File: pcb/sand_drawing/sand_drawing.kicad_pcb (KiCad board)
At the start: 2 copper layers, 34 parts, among them J0 12V GND, J1 Stepper1, J2 Stepper2, J3 Opto 1, J4 Opto 2, J5 UART, SW1 EN, SW2 IO0, U2 AMS1117-3.3, U3 ESP32-WROOM-32D

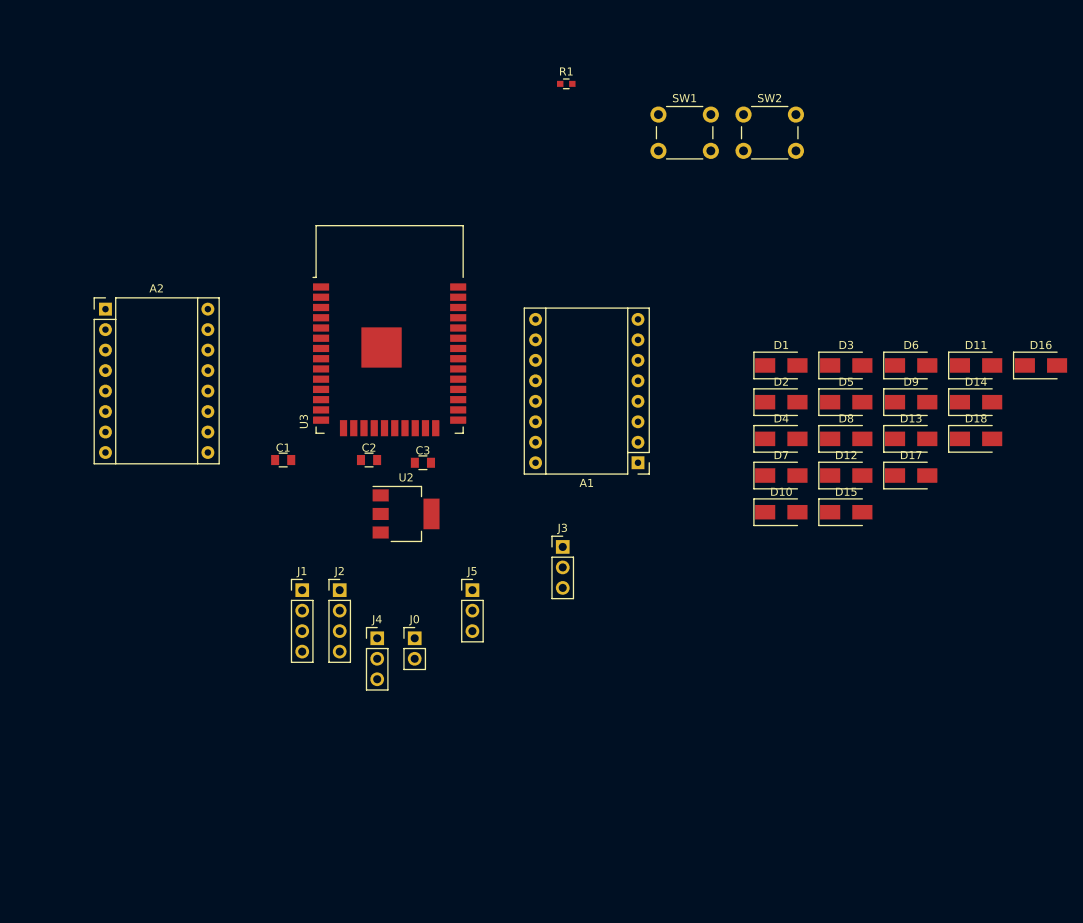
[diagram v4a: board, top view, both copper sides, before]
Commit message: Update BOM and beginning to lay out the new PCB.
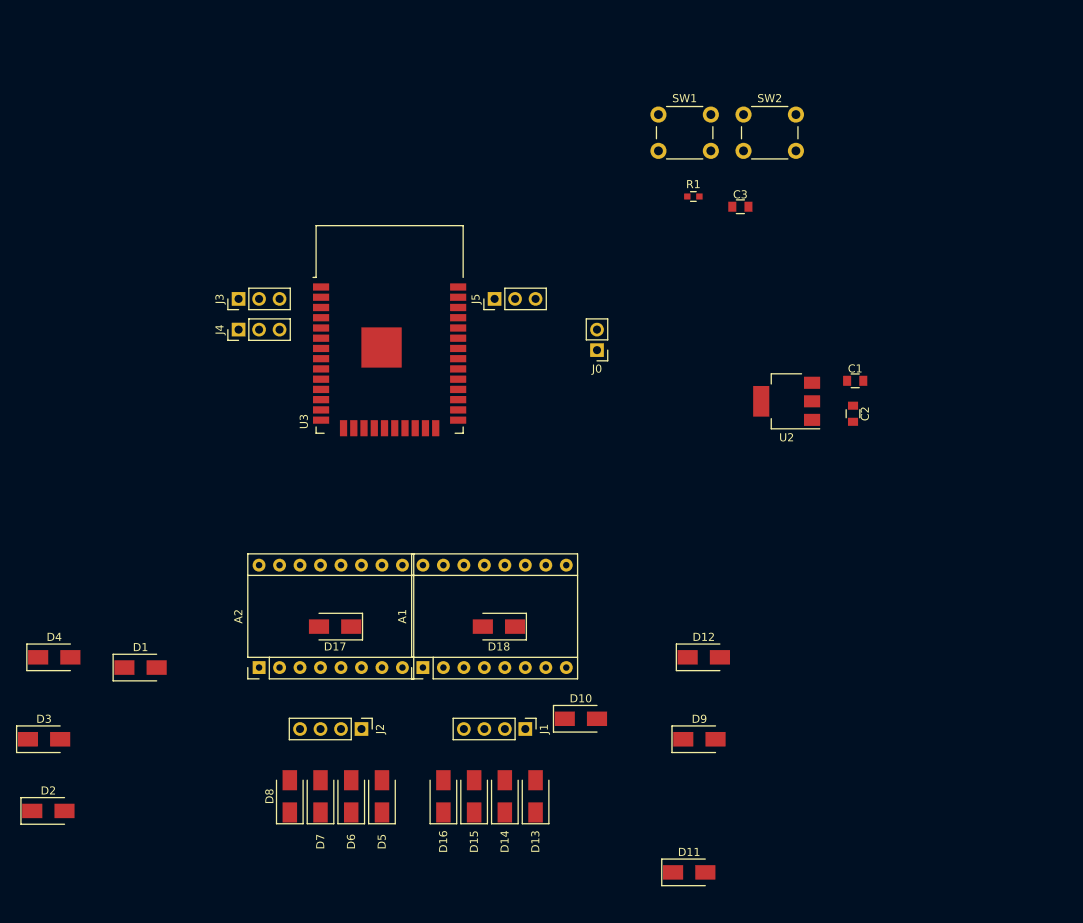
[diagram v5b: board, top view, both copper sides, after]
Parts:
- moved D3 109.8 mm to (81.3, 152.4)
- moved D2 104.1 mm to (81.8, 161.3)
- moved D4 94.2 mm to (82.5, 142.2)
- moved D16 91.4 mm to (130.8, 159.5), turned to 90 degrees
- moved D1 87.9 mm to (93.2, 143.5)
- moved D6 87.6 mm to (119.4, 159.5), turned to 90 degrees
- moved D8 82.0 mm to (111.8, 159.5), turned to 90 degrees
- moved D14 76.2 mm to (138.4, 159.5), turned to 90 degrees
- moved D5 75.5 mm to (123.2, 159.5), turned to 90 degrees
- moved D17 73.9 mm to (117.4, 138.4), turned to 180 degrees
- moved D11 72.2 mm to (161.3, 168.9)
- moved C1 71.6 mm to (181.9, 108.0)
- moved D7 69.6 mm to (115.6, 159.5), turned to 90 degrees
- moved D13 64.3 mm to (142.2, 159.5), turned to 90 degrees
- moved D18 63.6 mm to (137.7, 138.4), turned to 180 degrees
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
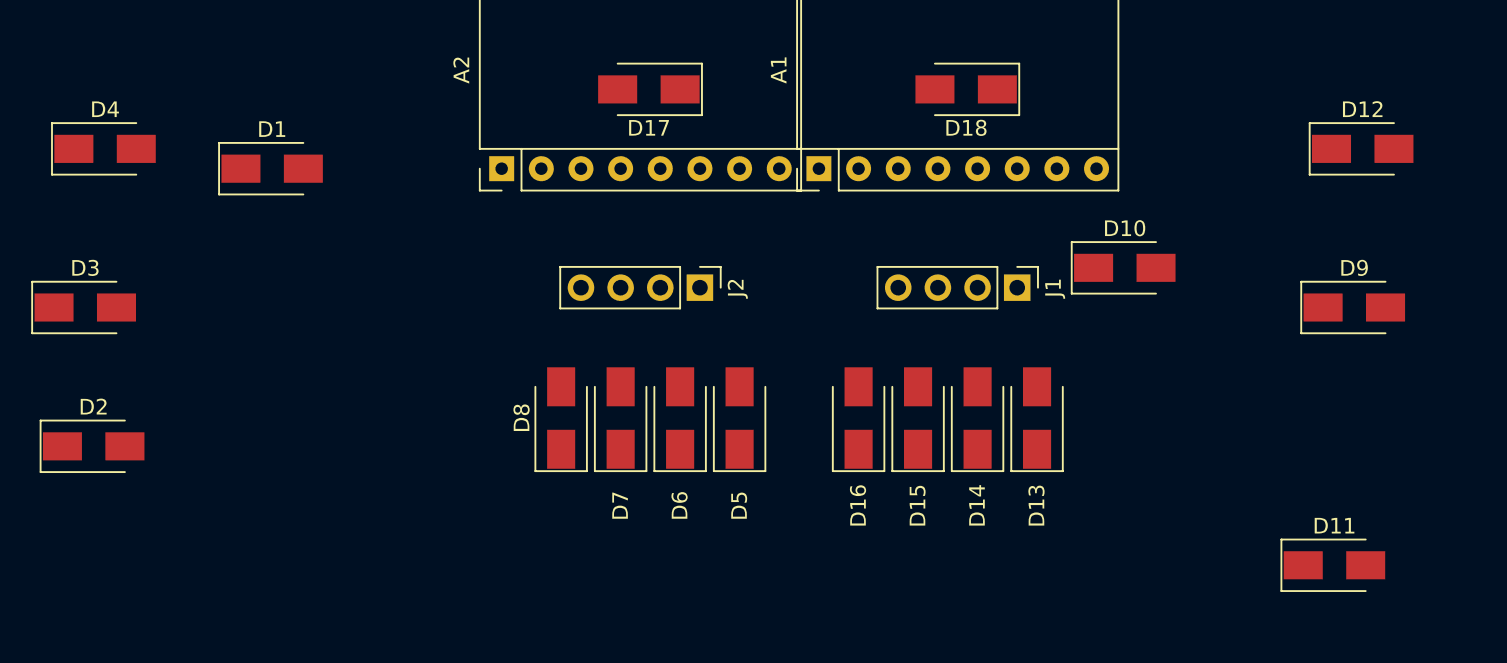
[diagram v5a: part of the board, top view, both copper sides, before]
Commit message: Protection diodes placed.
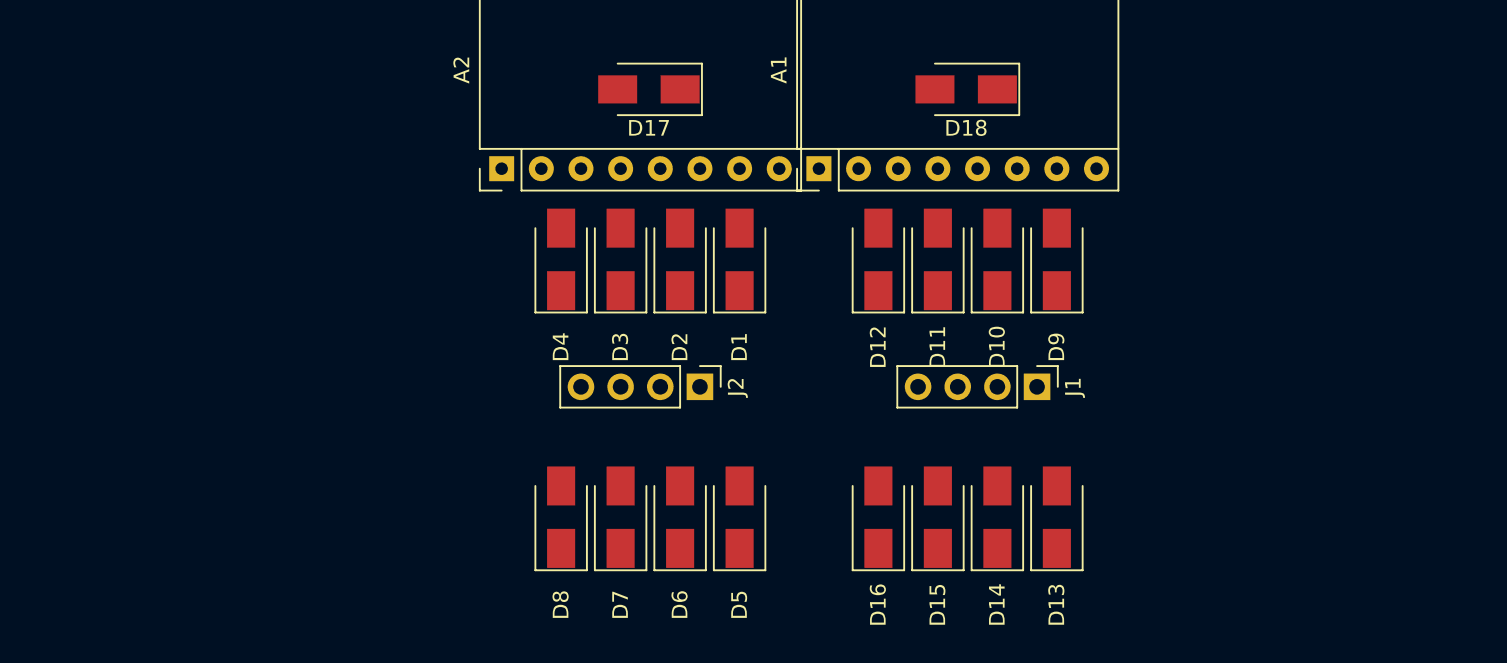
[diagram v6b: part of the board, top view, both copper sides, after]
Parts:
- moved D2 39.4 mm to (119.4, 149.3), turned to 90 degrees
- moved D3 34.4 mm to (115.6, 149.3), turned to 90 degrees
- moved D11 32.1 mm to (135.9, 149.3), turned to 90 degrees
- moved D12 31.8 mm to (132.1, 149.3), turned to 90 degrees
- moved D1 30.5 mm to (123.2, 149.3), turned to 90 degrees
- moved D4 30.1 mm to (111.8, 149.3), turned to 90 degrees
- moved D9 19.3 mm to (143.5, 149.3), turned to 90 degrees
- moved D10 8.18 mm to (139.7, 149.3), turned to 90 degrees
- moved D16 6.48 mm to (132.1, 165.8)
- moved D13 6.48 mm to (143.5, 165.8)
- moved D14 6.48 mm to (139.7, 165.8)
- moved D15 6.48 mm to (135.9, 165.8)
- moved J1 6.48 mm to (142.2, 157.5)
- moved D5 6.35 mm to (123.2, 165.8)
- moved D6 6.35 mm to (119.4, 165.8)
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
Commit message: Nearly finished PCB layout.
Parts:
- moved R1 62.4 mm to (103.0, 106.0), turned to 180 degrees
- moved SW1 60.0 mm to (102.2, 98.4)
- moved C3 56.4 mm to (112.4, 97.8), turned to 90 degrees
- moved C2 44.5 mm to (137.8, 104.1), turned to 90 degrees
- moved C1 37.7 mm to (144.8, 114.7), turned to 90 degrees
- moved U2 30.3 mm to (143.5, 105.4), turned to 0 degrees
- moved SW2 25.2 mm to (145.4, 86.0), turned to 270 degrees
- moved J0 14.1 mm to (141.6, 115.6)
- moved J4 12.3 mm to (102.9, 113.7)
- moved J3 12.3 mm to (102.9, 109.9)
- moved D1 10.3 mm to (119.4, 139.8)
- moved D10 10.3 mm to (135.9, 139.8)
- moved D12 10.3 mm to (128.3, 139.8)
- moved D13 10.3 mm to (139.7, 156.3)
- moved D14 10.3 mm to (135.9, 156.3)
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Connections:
- J3 pad 1: Net-(J3-Pad1) -> GND
- J4 pad 1: Net-(J3-Pad1) -> GND
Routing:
- net +12V: track 0.00 -> 178.1 mm
- net +3V3: track 0.00 -> 128.0 mm, vias 0 -> 6
- net Net-(SW2-Pad1): track 0.00 -> 40.4 mm
- net GND: track 0.00 -> 28.6 mm, vias 0 -> 9
- net D2Dir: track 0.00 -> 25.7 mm
- net Net-(A1-Pad6): track 0.00 -> 24.5 mm
- net Net-(A2-Pad6): track 0.00 -> 23.7 mm
- net Net-(A1-Pad3): track 0.00 -> 23.6 mm
- net Net-(A2-Pad3): track 0.00 -> 23.3 mm
- net D1Enable: track 0.00 -> 22.6 mm
- net Net-(A1-Pad4): track 0.00 -> 22.5 mm
- net Net-(A1-Pad5): track 0.00 -> 22.2 mm
- net Net-(A2-Pad5): track 0.00 -> 22.0 mm
- net D2Step: track 0.00 -> 22.0 mm
- net Net-(A2-Pad4): track 0.00 -> 21.5 mm
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
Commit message: Nearly finished PCB layout.
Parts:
- added REF**: MountingHole_3.2mm_M3, Mounting_Holes:MountingHole_3.2mm_M3, F.Cu at (95.5, 89.9)
- added REF**: MountingHole_3.2mm_M3, Mounting_Holes:MountingHole_3.2mm_M3, F.Cu at (152.4, 89.4)
- added REF**: MountingHole_3.2mm_M3, Mounting_Holes:MountingHole_3.2mm_M3, F.Cu at (99.1, 147.3)
- added REF**: MountingHole_3.2mm_M3, Mounting_Holes:MountingHole_3.2mm_M3, F.Cu at (147.4, 147.4)
- J0: footprint Socket_Strips:Socket_Strip_Straight_1x02_Pitch2.54mm -> Connectors_Phoenix:PhoenixContact_MCV-G_02x3.50mm_Vertical
- J1, J2: footprint Socket_Strips:Socket_Strip_Straight_1x04_Pitch2.54mm -> Connectors_Phoenix:PhoenixContact_MCV-G_04x3.50mm_Vertical
- J3, J4: footprint Socket_Strips:Socket_Strip_Straight_1x03_Pitch2.54mm -> Connectors_Phoenix:PhoenixContact_MCV-G_03x3.50mm_Vertical
- moved R1 10.5 mm to (103.4, 95.5)
- moved J3 8.68 mm to (100.2, 101.6), turned to 0 degrees
- moved SW1 5.52 mm to (102.6, 92.9), turned to 90 degrees
- moved C1 5.09 mm to (139.7, 114.3)
- moved J0 3.82 mm to (144.3, 112.8), turned to 270 degrees
- moved J4 2.93 mm to (100.1, 112.8), turned to 0 degrees
- moved J2 2.33 mm to (119.1, 147.3), turned to 180 degrees
- moved J1 0.71 mm to (138.8, 147.3), turned to 180 degrees
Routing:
- net GND: track 28.6 -> 41.2 mm
- net Net-(R1-Pad2): track 15.7 -> 9.15 mm
- net Net-(C3-Pad1): track 15.1 -> 17.5 mm
- net Net-(A2-Pad6): track 23.7 -> 21.6 mm
- net Net-(A1-Pad3): track 23.6 -> 21.5 mm
- net +12V: track 178.1 -> 179.9 mm
- net Net-(A2-Pad5): track 22.0 -> 21.0 mm
- net Opto2: track 17.6 -> 16.8 mm
- net Net-(A1-Pad4): track 22.5 -> 21.8 mm
- net Opto1: track 15.0 -> 14.3 mm
- net Net-(A2-Pad3): track 23.3 -> 22.8 mm
- net Net-(A1-Pad5): track 22.2 -> 22.7 mm
- net +3V3: track 128.0 -> 128.1 mm, vias 6 -> 5
